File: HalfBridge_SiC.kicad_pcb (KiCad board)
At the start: 2 copper layers, 100 x 100 mm, 37 parts, among them J1 Conn_02x08_Odd_Even, Q1 C3M0075120J, Q2 C3M0075120J, U1 TBA2-0522, U3 TBA2-0522, U4 NCD57252

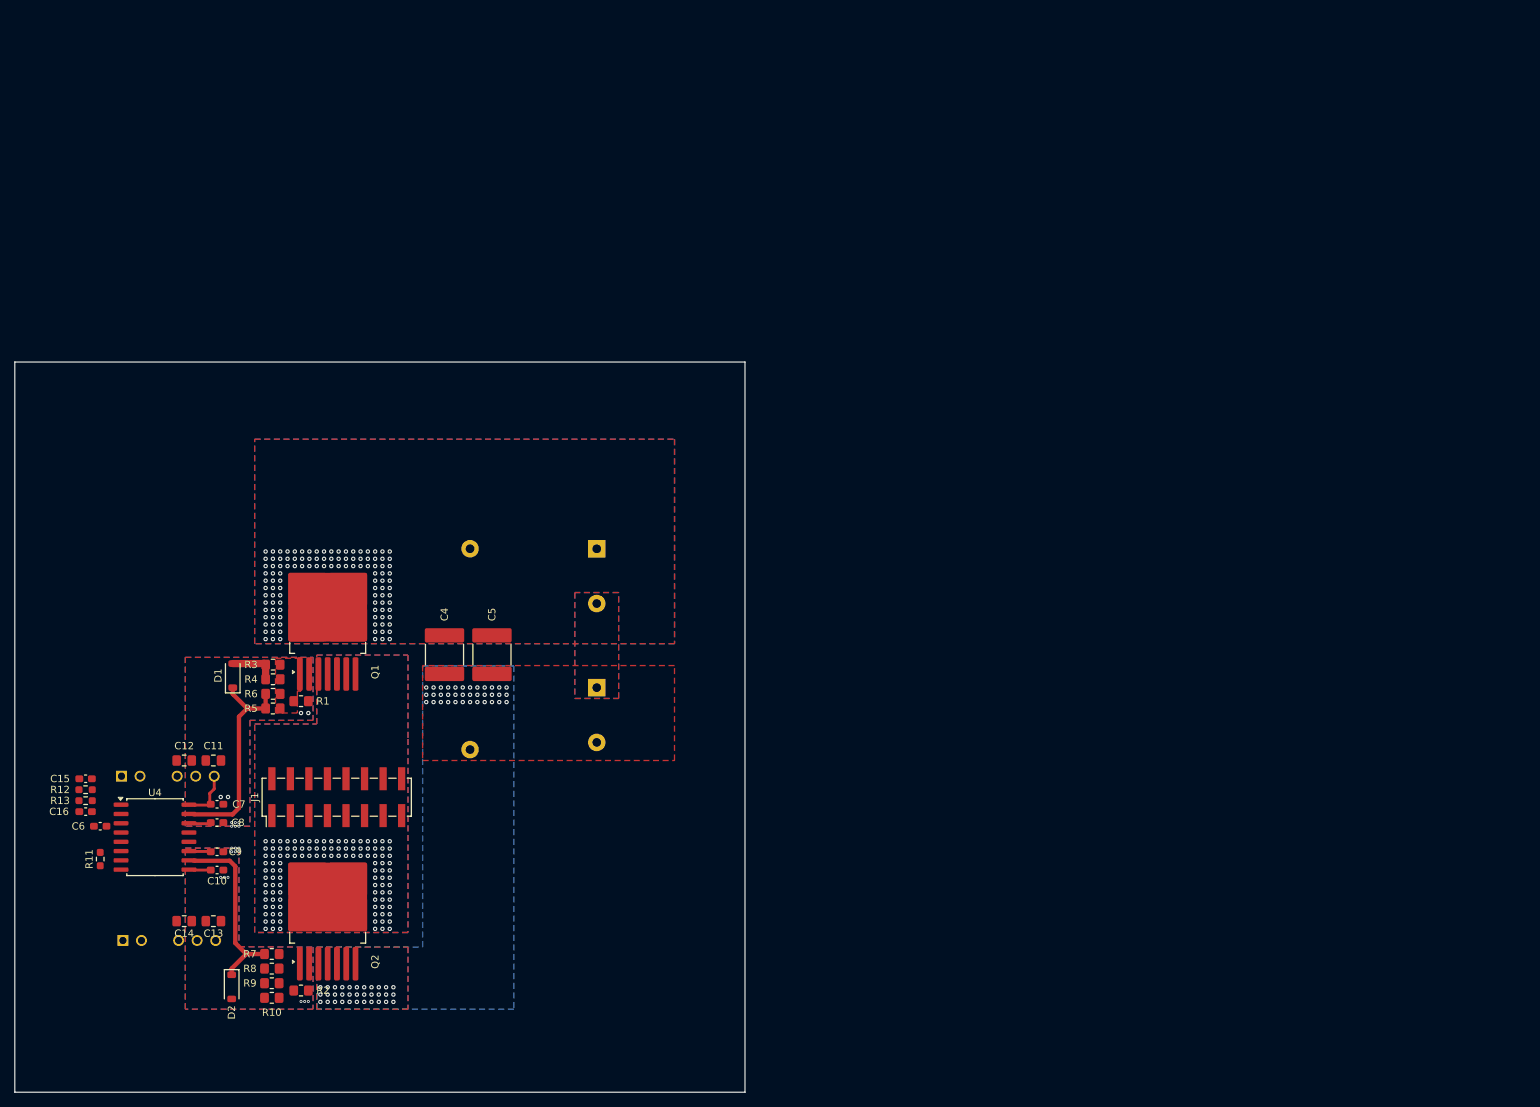
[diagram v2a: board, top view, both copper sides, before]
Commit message: switch dpdt 3d model
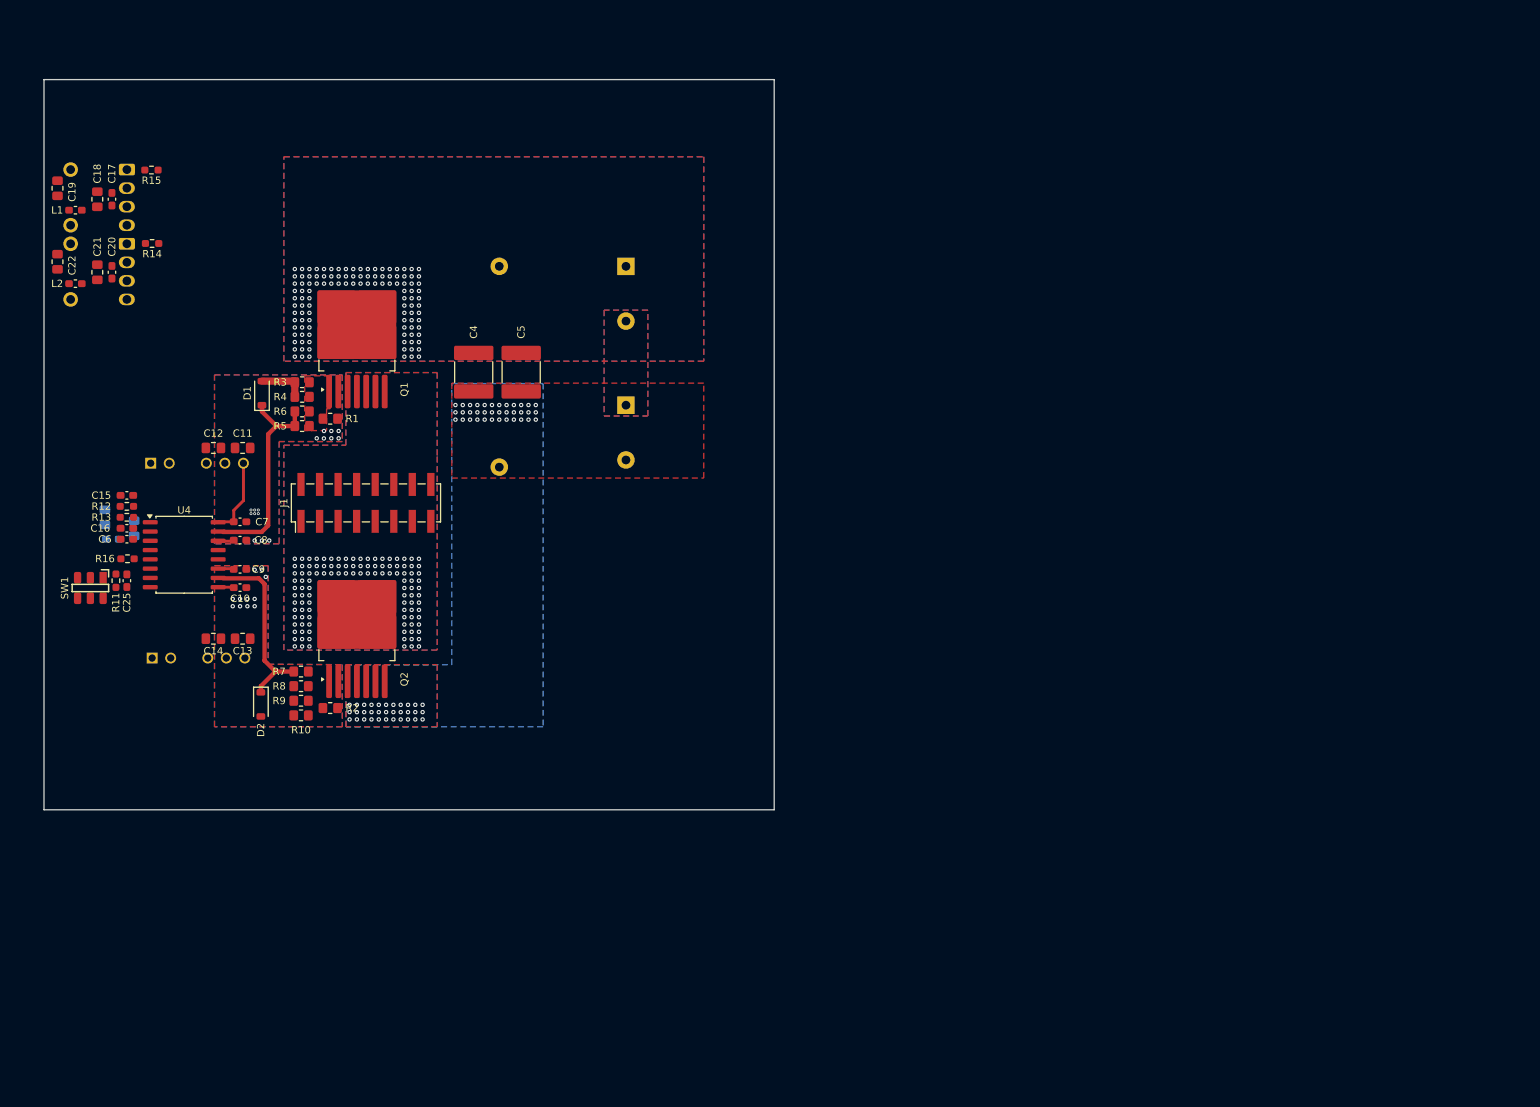
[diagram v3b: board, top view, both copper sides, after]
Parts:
- added C17: C, Capacitor_SMD:C_0603_1608Metric_Pad1.08x0.95mm_HandSolder, F.Cu at (48.5, 57.8)
- added C18: C, Capacitor_SMD:C_0805_2012Metric_Pad1.18x1.45mm_HandSolder, F.Cu at (46.5, 57.8)
- added C19: C, Capacitor_SMD:C_0805_2012Metric_Pad1.18x1.45mm_HandSolder, F.Cu at (41.0, 56.3)
- added C20: C, Capacitor_SMD:C_0603_1608Metric_Pad1.08x0.95mm_HandSolder, F.Cu at (48.5, 67.8)
- added C21: C, Capacitor_SMD:C_0805_2012Metric_Pad1.18x1.45mm_HandSolder, F.Cu at (46.5, 67.8)
- added C22: C, Capacitor_SMD:C_0805_2012Metric_Pad1.18x1.45mm_HandSolder, F.Cu at (41.0, 66.3)
- added C23: C, Capacitor_SMD:C_0805_2012Metric_Pad1.18x1.45mm_HandSolder, B.Cu at (47.5, 101.3)
- added C24: C, Capacitor_SMD:C_0805_2012Metric_Pad1.18x1.45mm_HandSolder, B.Cu at (51.5, 102.8)
- added C25: C, Capacitor_SMD:C_0603_1608Metric_Pad1.08x0.95mm_HandSolder, F.Cu at (50.5, 110.0)
- added J2: AFBR-2624Z, OptoDevice:Broadcom_AFBR-16xxZ_Horizontal, B.Cu at (50.5, 53.7)
- added J3: AFBR-2624Z, OptoDevice:Broadcom_AFBR-16xxZ_Horizontal, B.Cu at (50.5, 63.9)
- added L1: L, Inductor_SMD:L_0603_1608Metric_Pad1.05x0.95mm_HandSolder, F.Cu at (43.5, 59.3)
- added L2: L, Inductor_SMD:L_0603_1608Metric_Pad1.05x0.95mm_HandSolder, F.Cu at (43.5, 69.3)
- added L3: L, Inductor_SMD:L_0603_1608Metric_Pad1.05x0.95mm_HandSolder, B.Cu at (48.5, 104.3)
- added R14: R, Resistor_SMD:R_0603_1608Metric_Pad0.98x0.95mm_HandSolder, F.Cu at (54.0, 63.8)
- added R15: R, Resistor_SMD:R_0603_1608Metric_Pad0.98x0.95mm_HandSolder, F.Cu at (53.9, 53.8)
- added R16: R, Resistor_SMD:R_0603_1608Metric_Pad0.98x0.95mm_HandSolder, F.Cu at (50.6, 107.0)
- added SW1: CAS-D20X1, My_Button_Switch_SMD:Nidec_Copal_CAS-D20A1, F.Cu at (45.5, 111.0)
- C6: value C -> 100n
- moved U1 43.0 mm to (53.8, 93.9)
- moved C11 43.0 mm to (66.3, 91.8)
- moved C12 43.0 mm to (62.4, 91.8)
- moved J1 40.5 mm to (83.2, 99.3)
- moved C6 39.5 mm to (50.5, 104.3)
- moved C15 39.2 mm to (50.5, 98.3)
- moved C16 39.2 mm to (50.5, 102.8)
- moved R12 39.2 mm to (50.5, 99.8)
- moved R13 39.2 mm to (50.5, 101.3)
- moved C1 38.9 mm to (118.8, 66.9)
- moved C14 38.9 mm to (62.4, 117.9)
- moved C2 38.9 mm to (118.8, 86.0)
- moved C3 38.9 mm to (101.5, 66.9)
- moved C4 38.9 mm to (98.0, 81.4)
- moved C5 38.9 mm to (104.5, 81.4)
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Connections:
- R11 pad 1: /HalfBridge_GateDriver/dt -> /HalfBridge_GateDriver/gnd
- R11 pad 2: /HalfBridge_GateDriver/gnd -> /HalfBridge_GateDriver/rdt
- U4 pad 5: unconnected-(U4-DIS-Pad5) -> /HalfBridge_GateDriver/dis
- U4 pad 7: unconnected-(U4-ANB-Pad7) -> /HalfBridge_GateDriver/anb
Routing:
- net /HalfBridge_GateDriver/vddh: track 6.61 -> 10.7 mm
- net /HalfBridge_GateDriver/vssh: track 2.40 -> 1.55 mm
- net /HalfBridge_GateDriver/kl: vias 12 -> 11
- net /HalfBridge_GateDriver/kh: vias 10 -> 16
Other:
- board text added: "INA"
- board text added: "INB"

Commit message: dc dc 3d
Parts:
- removed C2: C, Capacitor_THT:CP_Radial_D18.0mm_P7.50mm
- removed C3: C, Capacitor_THT:C_Rect_L31.5mm_W15.0mm_P27.50mm_MKS4
- removed U3: TBA2-0522, Converter_DCDC:Converter_DCDC_TRACO_TBA2-xxxx_Dual_THT
- added D3: LED, LED_SMD:LED_0603_1608Metric_Pad1.05x0.95mm_HandSolder, F.Cu at (40.5, 83.0)
- added J4: Screw_Terminal_01x02, TerminalBlock_Phoenix:TerminalBlock_Phoenix_PT-1,5-2-3.5-H_1x02_P3.50mm_Horizontal, B.Cu at (44.5, 79.0)
- added R17: R, Resistor_SMD:R_0603_1608Metric, F.Cu at (43.0, 84.0)
- added U2: RKD-052005D, My_Converter_DCDC:Converter_DCDC_RECOM_RKZ-xx2005_Dual_THT_SIP7, B.Cu at (51.5, 120.5)
- C1: footprint Capacitor_THT:CP_Radial_D18.0mm_P7.50mm -> Capacitor_SMD:C_2220_5750Metric_Pad1.97x5.40mm_HandSolder; moved to F.Cu
- U1: value TBA2-0522 -> RKD-052005D; footprint Converter_DCDC:Converter_DCDC_TRACO_TBA2-xxxx_Dual_THT -> My_Converter_DCDC:Converter_DCDC_RECOM_RKZ-xx2005_Dual_THT_SIP7
- moved C1 16.5 mm to (111.0, 81.5)
- moved U1 3.44 mm to (51.5, 96.5)
- moved C23 3.18 mm to (47.5, 104.5)
- moved L3 2.32 mm to (50.5, 105.5)
- moved C11 2.09 mm to (66.3, 93.9)
- moved C12 2.09 mm to (62.4, 93.9)
- moved J1 2.04 mm to (82.3, 97.5)
- moved Q2 1.62 mm to (82.0, 114.5)
- moved D2 1.58 mm to (69.5, 125.5)
- moved R10 1.45 mm to (74.5, 127.0)
- moved R2 1.45 mm to (78.5, 126.0)
- moved R7 1.45 mm to (74.5, 121.0)
- moved R8 1.45 mm to (74.5, 123.0)
- moved R9 1.45 mm to (74.5, 125.0)
- moved C24 1.21 mm to (50.5, 103.5), turned to 180 degrees
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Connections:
- C1 pad 2: /HalfBridge_Power/dcm -> /HalfBridge_Power/dcn
- U1 pad 1: unconnected-(U1-+Vin-Pad1) -> Net-(U1-VIN+)
- U1 pad 2: unconnected-(U1--Vin-Pad2) -> Net-(U1-VIN-)
- U1 pad 5: unconnected-(U1-Com-Pad5) -> /HalfBridge_GateDriver/vssh
- U1 pad 6: /HalfBridge_GateDriver/vddh -> unconnected-(U1-COM-Pad6)
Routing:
- net /HalfBridge_GateDriver/gonh: track 28.8 -> 7.32 mm
- net /HalfBridge_GateDriver/vddh: track 10.7 -> 2.16 mm
- net /HalfBridge_GateDriver/asgl: track 0.21 -> 4.27 mm
- net /HalfBridge_GateDriver/gonl: track 24.8 -> 27.0 mm
- net /HalfBridge_Power/ph: vias 114 -> 160
- net /HalfBridge_Power/dcp: vias 114 -> 160
- net /HalfBridge_GateDriver/kl: vias 11 -> 19
- net /HalfBridge_GateDriver/kh: vias 16 -> 14
- added copper zone on B.Cu, net (none)
- added copper zone on F.Cu, net (none)
- added copper zone on F.Cu, net /HalfBridge_Power/gl
- removed copper zone on B.Cu, net /HalfBridge_Power/dcm
- removed copper zone on F.Cu, net /HalfBridge_Power/dcm
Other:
- board text added: "GND 5V"

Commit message: position
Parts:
- moved C12 1.86 mm to (60.5, 93.7)
- moved C14 1.86 mm to (60.1, 117.3)
- moved C15 1.86 mm to (48.6, 98.1)
- moved C16 1.86 mm to (48.6, 102.6)
- moved C23 1.86 mm to (45.6, 104.3)
- moved C24 1.86 mm to (48.6, 103.3)
- moved C25 1.86 mm to (48.6, 109.8)
- moved C6 1.86 mm to (48.6, 104.1)
- moved L3 1.86 mm to (48.6, 105.3)
- moved R11 1.86 mm to (47.1, 109.8)
- moved R12 1.86 mm to (48.6, 99.6)
- moved R13 1.86 mm to (48.6, 101.1)
- moved R16 1.86 mm to (48.7, 106.8)
- moved SW1 1.86 mm to (43.6, 110.8)
- moved U1 1.86 mm to (49.6, 96.3)
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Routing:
- net /HalfBridge_GateDriver/gonl: track 27.0 -> 8.26 mm

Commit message: diff rx
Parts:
- added J5: Conn_01x04, Connector_Molex:Molex_PicoBlade_53261-0471_1x04-1MP_P1.25mm_Horizontal, F.Cu at (45.0, 91.0)
- added SW2: CAS-D20X1, My_Button_Switch_SMD:Nidec_Copal_CAS-D20A1, F.Cu at (51.5, 77.0)
- added U3: MAX3284E, Package_TO_SOT_SMD:SOT-23-6_Handsoldering, F.Cu at (51.9, 92.5)
- added U5: MAX3284E, Package_TO_SOT_SMD:SOT-23-6_Handsoldering, F.Cu at (51.9, 89.0)
- moved C20 12.3 mm to (49.5, 55.5)
- moved C21 12.3 mm to (47.5, 55.5)
- moved J3 12.3 mm to (51.5, 51.6)
- moved R14 12.3 mm to (55.0, 51.6)
- moved C22 12.3 mm to (42.0, 54.1)
- moved L2 12.3 mm to (44.5, 57.1)
- moved C17 8.27 mm to (49.5, 66.0)
- moved C18 8.27 mm to (47.5, 66.0)
- moved C19 8.27 mm to (42.0, 64.5)
- moved L1 8.27 mm to (44.5, 67.5)
- moved J2 8.27 mm to (51.5, 61.9)
- moved R15 8.27 mm to (54.9, 62.0)
- moved C11 6.95 mm to (66.0, 100.5)
- moved C12 6.95 mm to (62.0, 100.5)
- moved C24 6.75 mm to (49.5, 110.0)
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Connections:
- net /HalfBridge_GateDriver/gnd renamed /HalfBridge_Diff/gnd
- net /HalfBridge_GateDriver/vcc renamed /HalfBridge_Diff/vcc
- C17 pad 1: /HalfBridge_Optical/vcca -> /HalfBridge_Optical/vccb
- C18 pad 1: /HalfBridge_Optical/vcca -> /HalfBridge_Optical/vccb
- C20 pad 1: /HalfBridge_Optical/vccb -> /HalfBridge_Optical/vcca
- C21 pad 1: /HalfBridge_Optical/vccb -> /HalfBridge_Optical/vcca
- J2 pad 1: /HalfBridge_Optical/xna -> /HalfBridge_Optical/xnb
- J2 pad 3: /HalfBridge_Optical/vcca -> /HalfBridge_Optical/vccb
- J3 pad 1: /HalfBridge_Optical/xnb -> /HalfBridge_Optical/xna
- J3 pad 3: /HalfBridge_Optical/vccb -> /HalfBridge_Optical/vcca
- L1 pad 1: /HalfBridge_Optical/vcca -> /HalfBridge_Optical/vccb
- L2 pad 1: /HalfBridge_Optical/vccb -> /HalfBridge_Optical/vcca
- R14 pad 1: /HalfBridge_GateDriver/inb -> /HalfBridge_Optical/ina
- R14 pad 2: /HalfBridge_Optical/xnb -> /HalfBridge_Optical/xna
- R15 pad 1: /HalfBridge_GateDriver/ina -> /HalfBridge_Optical/inb
- R15 pad 2: /HalfBridge_Optical/xna -> /HalfBridge_Optical/xnb
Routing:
- net /HalfBridge_GateDriver/inb: track 0.00 -> 44.9 mm
- net /HalfBridge_Optical/ina: track 0.00 -> 35.6 mm
- net /HalfBridge_GateDriver/ina: track 0.00 -> 35.4 mm
- net /HalfBridge_Diff/vcc: track 0.00 -> 33.7 mm
- net /HalfBridge_Optical/inb: track 0.00 -> 20.2 mm
- net /HalfBridge_Diff/ina_d: track 0.00 -> 17.0 mm
- net /HalfBridge_GateDriver/gonl: track 8.26 -> 24.8 mm
- net /HalfBridge_Diff/inb_d: track 0.00 -> 15.4 mm
- net /HalfBridge_GateDriver/kl: vias 19 -> 24
- net /HalfBridge_GateDriver/kh: vias 14 -> 15
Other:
- board size 100 x 100 mm -> 100 x 100.3 mm
- board text added: "INA PWM"
- board text removed: "INA"

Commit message: quad diff receiver
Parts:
- added C2: 100n, Capacitor_SMD:C_0603_1608Metric_Pad1.08x0.95mm_HandSolder, F.Cu at (54.0, 86.5)
- added C26: 100n, Capacitor_SMD:C_0603_1608Metric_Pad1.08x0.95mm_HandSolder, F.Cu at (62.6, 79.5)
- added C3: 100n, Capacitor_SMD:C_0603_1608Metric_Pad1.08x0.95mm_HandSolder, F.Cu at (54.0, 81.0)
- added R18: R, Resistor_SMD:R_0603_1608Metric_Pad0.98x0.95mm_HandSolder, B.Cu at (48.0, 85.5)
- added R19: R, Resistor_SMD:R_0603_1608Metric_Pad0.98x0.95mm_HandSolder, B.Cu at (48.0, 80.0)
- added SW3: CAS-D20X1, My_Button_Switch_SMD:Nidec_Copal_CAS-D20A1, F.Cu at (44.1, 94.8)
- added U6: 74AUC2GU04, Package_TO_SOT_SMD:SOT-23-6_Handsoldering, F.Cu at (50.6, 74.5)
- J5: value Conn_01x04 -> Conn_01x04_Shielded; footprint Connector_Molex:Molex_PicoBlade_53261-0471_1x04-1MP_P1.25mm_Horizontal -> My_Connector:Samtec_T1M-04-X-SH-L_1x04-1SH_P1.0mm_Terminal_Horizontal_Latch
- moved J4 53.8 mm to (45.2, 130.8)
- moved D3 42.0 mm to (43.0, 123.0)
- moved R17 42.0 mm to (45.3, 124.0)
- moved J5 10.0 mm to (44.0, 81.0)
- moved U5 9.02 mm to (50.7, 80.0)
- moved SW2 7.83 mm to (44.5, 73.5)
- moved U3 7.15 mm to (50.6, 85.5)
- moved U2 3.31 mm to (50.5, 119.5)
- moved C14 2.33 mm to (61.5, 117.5), turned to 180 degrees
- moved C13 2.31 mm to (65.5, 117.5), turned to 0 degrees
- moved C19 0.46 mm to (42.5, 64.5)
- moved C22 0.45 mm to (42.5, 54.1)
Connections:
- U3 pad 3: /HalfBridge_Diff/ina_d -> /HalfBridge_Diff/ina_nd
- U5 pad 3: /HalfBridge_Diff/inb_d -> /HalfBridge_Diff/inb_nd
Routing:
- net /HalfBridge_Diff/vcc: track 33.7 -> 96.3 mm
- net /HalfBridge_GateDriver/inb: track 44.9 -> 7.70 mm
- net /HalfBridge_GateDriver/ina: track 35.4 -> 5.50 mm
- net /HalfBridge_Diff/ina_d: track 17.0 -> 0.00 mm
- net /HalfBridge_Diff/inb_d: track 15.4 -> 0.00 mm
- net /HalfBridge_Optical/inb: track 20.2 -> 8.67 mm
- net /HalfBridge_Optical/ina: track 35.6 -> 25.3 mm
- net /HalfBridge_Diff/inb_db: vias 0 -> 1
- net /HalfBridge_Diff/inb_da: vias 0 -> 1
- net /HalfBridge_Diff/ina_db: vias 0 -> 1
- net /HalfBridge_Diff/ina_da: vias 0 -> 1

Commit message: not gate
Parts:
- moved C26 6.77 mm to (56.5, 76.6), turned to 90 degrees
- moved U6 2.61 mm to (53.0, 75.5)
- moved SW2 1.58 mm to (45.0, 75.0), turned to 180 degrees
- moved J5 1.50 mm to (44.0, 82.5)
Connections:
- U6 pad 1: /HalfBridge_Diff/ina_nd -> /HalfBridge_Diff/inb_nd
- U6 pad 3: /HalfBridge_Diff/inb_nd -> /HalfBridge_Diff/ina_nd
- U6 pad 4: /HalfBridge_Diff/inb_d -> /HalfBridge_Diff/ina_d
- U6 pad 6: /HalfBridge_Diff/ina_d -> /HalfBridge_Diff/inb_d
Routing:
- net /HalfBridge_Diff/vcc: track 96.3 -> 152.6 mm
- net /HalfBridge_Diff/inb_d: track 0.00 -> 12.5 mm
- net /HalfBridge_Optical/inb: track 8.67 -> 20.7 mm
- net /HalfBridge_GateDriver/inb: track 7.70 -> 17.9 mm
- net /HalfBridge_Diff/ina_nd: track 0.00 -> 9.15 mm
- net /HalfBridge_Optical/ina: track 25.3 -> 31.2 mm
- net /HalfBridge_Diff/inb_nd: track 0.00 -> 5.86 mm
- net /HalfBridge_GateDriver/ina: track 5.50 -> 10.2 mm
